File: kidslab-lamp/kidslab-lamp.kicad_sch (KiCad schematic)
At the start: 41 parts, among them U1 Pico

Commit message: adding components to schematic
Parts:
- removed C1, C3: pin_header_1x3, Connector_PinHeader_2.54mm:PinHeader_1x03_P2.54mm_Vertical, symbol kidslab:pin_header_1x3
- removed C2: 114020163, kidslab:114020163, symbol kidslab:114020163
- removed D12: SK6812, LED_SMD:LED_SK6812_PLCC4_5.0x5.0mm_P3.2mm, symbol LED:SK6812
- removed GPIO0, GPIO1, GPIO21, GPIO22, GPIO26, GPIO27, GPIO28: kroko_edge, kidslab:Edgeconnector, symbol kidslab:kroko_edge
- removed GPIO13, GPIO18: kroko_board, kidslab:KrokoConnector, symbol kidslab:kroko_board
- removed GPIO14, GPIO15, GPIO16, GPIO17: arrow, kidslab:Kroko_Arrow, symbol kidslab:arrow
- removed R1, R2, R3, R4: 10M, Resistor_THT:R_Axial_DIN0204_L3.6mm_D1.6mm_P5.08mm_Horizontal, symbol Device:R
- added GPIO1, GPIO16: kroko_board, kidslab:KrokoConnector, symbol kidslab:kroko_board
- added GPIO10, GPIO11, GPIO12, GPIO13, GPIO14, GPIO15, GPIO9: kroko_edge, kidslab:Edgeconnector, symbol kidslab:kroko_edge
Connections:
- net at U1.24 (GPIO18): now also GPIO16.1
- net at U1.29 (GPIO22): now also GPIO14.1
- net at U1.1 (GPIO0): now also GPIO2.1
- net GPIO7/SCL1: now reaches U1.10 (GPIO7)
- net at U1.17 (GPIO13): now also GPIO1.1
- net at U1.2 (GPIO1): now also GPIO3.1
- net GPIO20/Buzzer: now reaches U1.26 (GPIO20)
- net at U1.27 (GPIO21): now also GPIO15.1
- net at U1.31 (GPIO26_ADC0): now also GPIO13.1
- net at U1.32 (GPIO27_ADC1): now also GPIO12.1
- net at U1.34 (GPIO28_ADC2): now also GPIO11.1
- net at U1.4 (GPIO2): now also GPIO4.1; no longer GPIO2.1
- net at U1.5 (GPIO3): now also GPIO9.1; no longer GPIO3.1
- net at U1.6 (GPIO4): now also GPIO10.1; no longer GPIO4.1
- net GPIO5/INTR: now reaches U1.7 (GPIO5)
- net GPIO6/SDA1: now reaches U1.9 (GPIO6)
- net 3.3V renamed +3V3
- net V_BUS renamed +5V
- net grove_rx renamed GPIO9/GROVE_RX
- net grove_tx renamed GPIO8/GROVE_TX
- no-connect marks 6 -> 9
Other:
- added sheet Components (components-sheet.kicad_sch)
- note added: "3V3 Output"
- note added: "5V Input"
- note added: "GND Output"
- note added: "Power-Groko-Anschlüsse"
- note added: "nicht mehr als 300 mA !"
- note removed: "(5 V)"
- note removed: "Grove"
- note removed: "LED"
- note removed: "Pfeiltasten"
- note removed: "Power-Groko"
- note removed: "Servo-Anschlüsse"
- moved on the sheet: B1, B2, B3, B4, B5, B6, E30, E31, E32, E33, E34, E35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

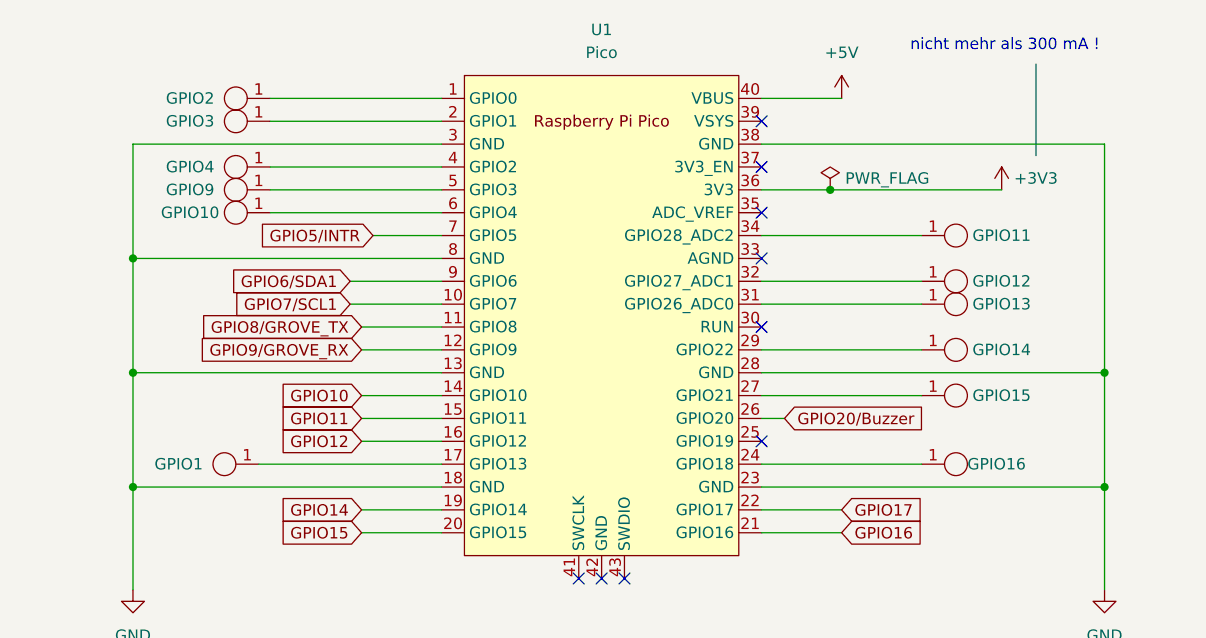
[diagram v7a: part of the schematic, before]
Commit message: adding layout
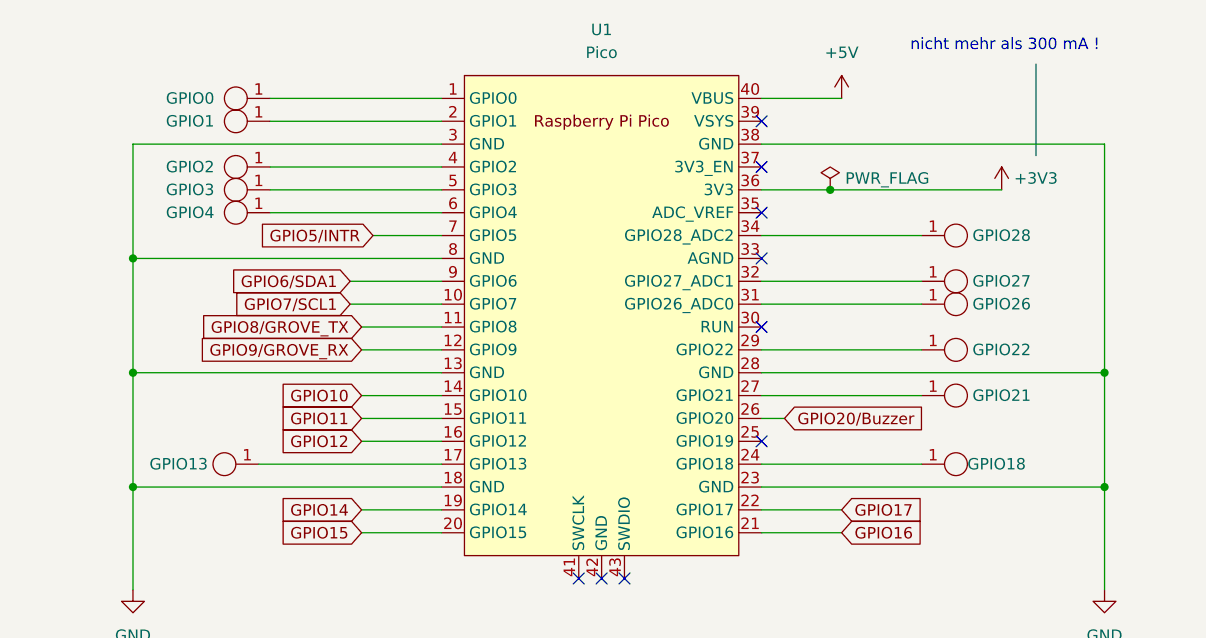
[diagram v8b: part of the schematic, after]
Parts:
- U1: now left out of the parts list
- renumbered GPIO2 to GPIO0, GPIO3 to GPIO1, GPIO1 to GPIO13, GPIO16 to GPIO18, GPIO4 to GPIO2, GPIO15 to GPIO21, GPIO14 to GPIO22, GPIO13 to GPIO26, GPIO12 to GPIO27, GPIO11 to GPIO28, GPIO9 to GPIO3, GPIO10 to GPIO4
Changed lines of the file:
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@@
   (symbol (lib_id "kidslab:kroko_edge") (at 121.92 57.15 0) (unit 1)
     (in_bom no) (on_board yes) (dnp no)
-    (property "Reference" "GPIO13" (at 128.27 57.15 0)
+    (property "Reference" "GPIO26" (at 128.27 57.15 0)
       (effects (font (size 1.27 1.27)))
     )
@@
       (project "kidslab-lamp"
         (path "/3a714d6a-4fcb-43e8-9668-1af7c84d4f32"
-          (reference "GPIO13") (unit 1)
+          (reference "GPIO26") (unit 1)
         )
       )
@@
   (symbol (lib_id "kidslab:kroko_edge") (at 44.45 41.91 180) (unit 1)
     (in_bom no) (on_board yes) (dnp no)
-    (property "Reference" "GPIO4" (at 38.1 41.91 0)
+    (property "Reference" "GPIO2" (at 38.1 41.91 0)
       (effects (font (size 1.27 1.27)))
     )
@@
       (project "kidslab-lamp"
         (path "/3a714d6a-4fcb-43e8-9668-1af7c84d4f32"
-          (reference "GPIO4") (unit 1)
+          (reference "GPIO2") (unit 1)
         )
       )
@@
   )
   (symbol (lib_id "pi-pico:Pico") (at 83.82 58.42 0) (unit 1)
-    (in_bom yes) (on_board yes) (dnp no) (fields_autoplaced)
+    (in_bom no) (on_board yes) (dnp no) (fields_autoplaced)
     (property "Reference" "U1" (at 83.82 26.67 0)
       (effects (font (size 1.27 1.27)))
@@
   (symbol (lib_id "kidslab:kroko_edge") (at 121.92 49.53 0) (unit 1)
     (in_bom no) (on_board yes) (dnp no)
-    (property "Reference" "GPIO11" (at 128.27 49.53 0)
+    (property "Reference" "GPIO28" (at 128.27 49.53 0)
       (effects (font (size 1.27 1.27)))
     )
@@
       (project "kidslab-lamp"
         (path "/3a714d6a-4fcb-43e8-9668-1af7c84d4f32"
-          (reference "GPIO11") (unit 1)
+          (reference "GPIO28") (unit 1)
         )
       )
@@
   (symbol (lib_id "kidslab:kroko_edge") (at 44.45 36.83 180) (unit 1)
     (in_bom no) (on_board yes) (dnp no)
-    (property "Reference" "GPIO3" (at 38.1 36.83 0)
+    (property "Reference" "GPIO1" (at 38.1 36.83 0)
       (effects (font (size 1.27 1.27)))
     )
@@
       (project "kidslab-lamp"
         (path "/3a714d6a-4fcb-43e8-9668-1af7c84d4f32"
-          (reference "GPIO3") (unit 1)
+          (reference "GPIO1") (unit 1)
         )
       )
@@
   (symbol (lib_id "kidslab:kroko_edge") (at 44.45 34.29 180) (unit 1)
     (in_bom no) (on_board yes) (dnp no)
-    (property "Reference" "GPIO2" (at 38.1 34.29 0)
+    (property "Reference" "GPIO0" (at 38.1 34.29 0)
       (effects (font (size 1.27 1.27)))
     )
@@
       (project "kidslab-lamp"
         (path "/3a714d6a-4fcb-43e8-9668-1af7c84d4f32"
-          (reference "GPIO2") (unit 1)
+          (reference "GPIO0") (unit 1)
         )
       )
@@
   (symbol (lib_id "kidslab:kroko_board") (at 43.18 74.93 180) (unit 1)
     (in_bom no) (on_board yes) (dnp no)
-    (property "Reference" "GPIO1" (at 36.83 74.93 0)
+    (property "Reference" "GPIO13" (at 36.83 74.93 0)
       (effects (font (size 1.27 1.27)))
     )
@@
       (project "kidslab-lamp"
         (path "/3a714d6a-4fcb-43e8-9668-1af7c84d4f32"
-          (reference "GPIO1") (unit 1)
+          (reference "GPIO13") (unit 1)
         )
       )
@@
   (symbol (lib_id "kidslab:kroko_edge") (at 44.45 44.45 180) (unit 1)
     (in_bom no) (on_board yes) (dnp no)
-    (property "Reference" "GPIO9" (at 38.1 44.45 0)
+    (property "Reference" "GPIO3" (at 38.1 44.45 0)
       (effects (font (size 1.27 1.27)))
     )
@@
       (project "kidslab-lamp"
         (path "/3a714d6a-4fcb-43e8-9668-1af7c84d4f32"
-          (reference "GPIO9") (unit 1)
+          (reference "GPIO3") (unit 1)
         )
       )
@@
   (symbol (lib_id "kidslab:kroko_edge") (at 121.92 62.23 0) (unit 1)
     (in_bom no) (on_board yes) (dnp no)
-    (property "Reference" "GPIO14" (at 128.27 62.23 0)
+    (property "Reference" "GPIO22" (at 128.27 62.23 0)
       (effects (font (size 1.27 1.27)))
     )
@@
       (project "kidslab-lamp"
         (path "/3a714d6a-4fcb-43e8-9668-1af7c84d4f32"
-          (reference "GPIO14") (unit 1)
+          (reference "GPIO22") (unit 1)
         )
       )
@@
   (symbol (lib_id "kidslab:kroko_board") (at 121.92 74.93 0) (unit 1)
     (in_bom no) (on_board yes) (dnp no)
-    (property "Reference" "GPIO16" (at 124.46 74.93 0)
+    (property "Reference" "GPIO18" (at 124.46 74.93 0)
       (effects (font (size 1.27 1.27)) (justify left))
     )
@@
       (project "kidslab-lamp"
         (path "/3a714d6a-4fcb-43e8-9668-1af7c84d4f32"
-          (reference "GPIO16") (unit 1)
+          (reference "GPIO18") (unit 1)
         )
       )
@@
   (symbol (lib_id "kidslab:kroko_edge") (at 44.45 46.99 180) (unit 1)
     (in_bom no) (on_board yes) (dnp no)
-    (property "Reference" "GPIO10" (at 38.1 46.99 0)
+    (property "Reference" "GPIO4" (at 38.1 46.99 0)
       (effects (font (size 1.27 1.27)))
     )
@@
       (project "kidslab-lamp"
         (path "/3a714d6a-4fcb-43e8-9668-1af7c84d4f32"
-          (reference "GPIO10") (unit 1)
+          (reference "GPIO4") (unit 1)
         )
       )
@@
   (symbol (lib_id "kidslab:kroko_edge") (at 121.92 67.31 0) (unit 1)
     (in_bom no) (on_board yes) (dnp no)
-    (property "Reference" "GPIO15" (at 128.27 67.31 0)
+    (property "Reference" "GPIO21" (at 128.27 67.31 0)
       (effects (font (size 1.27 1.27)))
     )
@@
       (project "kidslab-lamp"
         (path "/3a714d6a-4fcb-43e8-9668-1af7c84d4f32"
-          (reference "GPIO15") (unit 1)
+          (reference "GPIO21") (unit 1)
         )
       )
@@
   (symbol (lib_id "kidslab:kroko_edge") (at 121.92 54.61 0) (unit 1)
     (in_bom no) (on_board yes) (dnp no)
-    (property "Reference" "GPIO12" (at 128.27 54.61 0)
+    (property "Reference" "GPIO27" (at 128.27 54.61 0)
       (effects (font (size 1.27 1.27)))
     )
@@
       (project "kidslab-lamp"
         (path "/3a714d6a-4fcb-43e8-9668-1af7c84d4f32"
-          (reference "GPIO12") (unit 1)
-        )
-      )
+          (reference "GPIO27") (unit 1)
+        )
+      )
